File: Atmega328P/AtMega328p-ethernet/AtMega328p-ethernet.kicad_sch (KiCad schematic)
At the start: 14 parts, among them SW1 SW_Push, U1 ATmega328P-A, Y1 Crystal

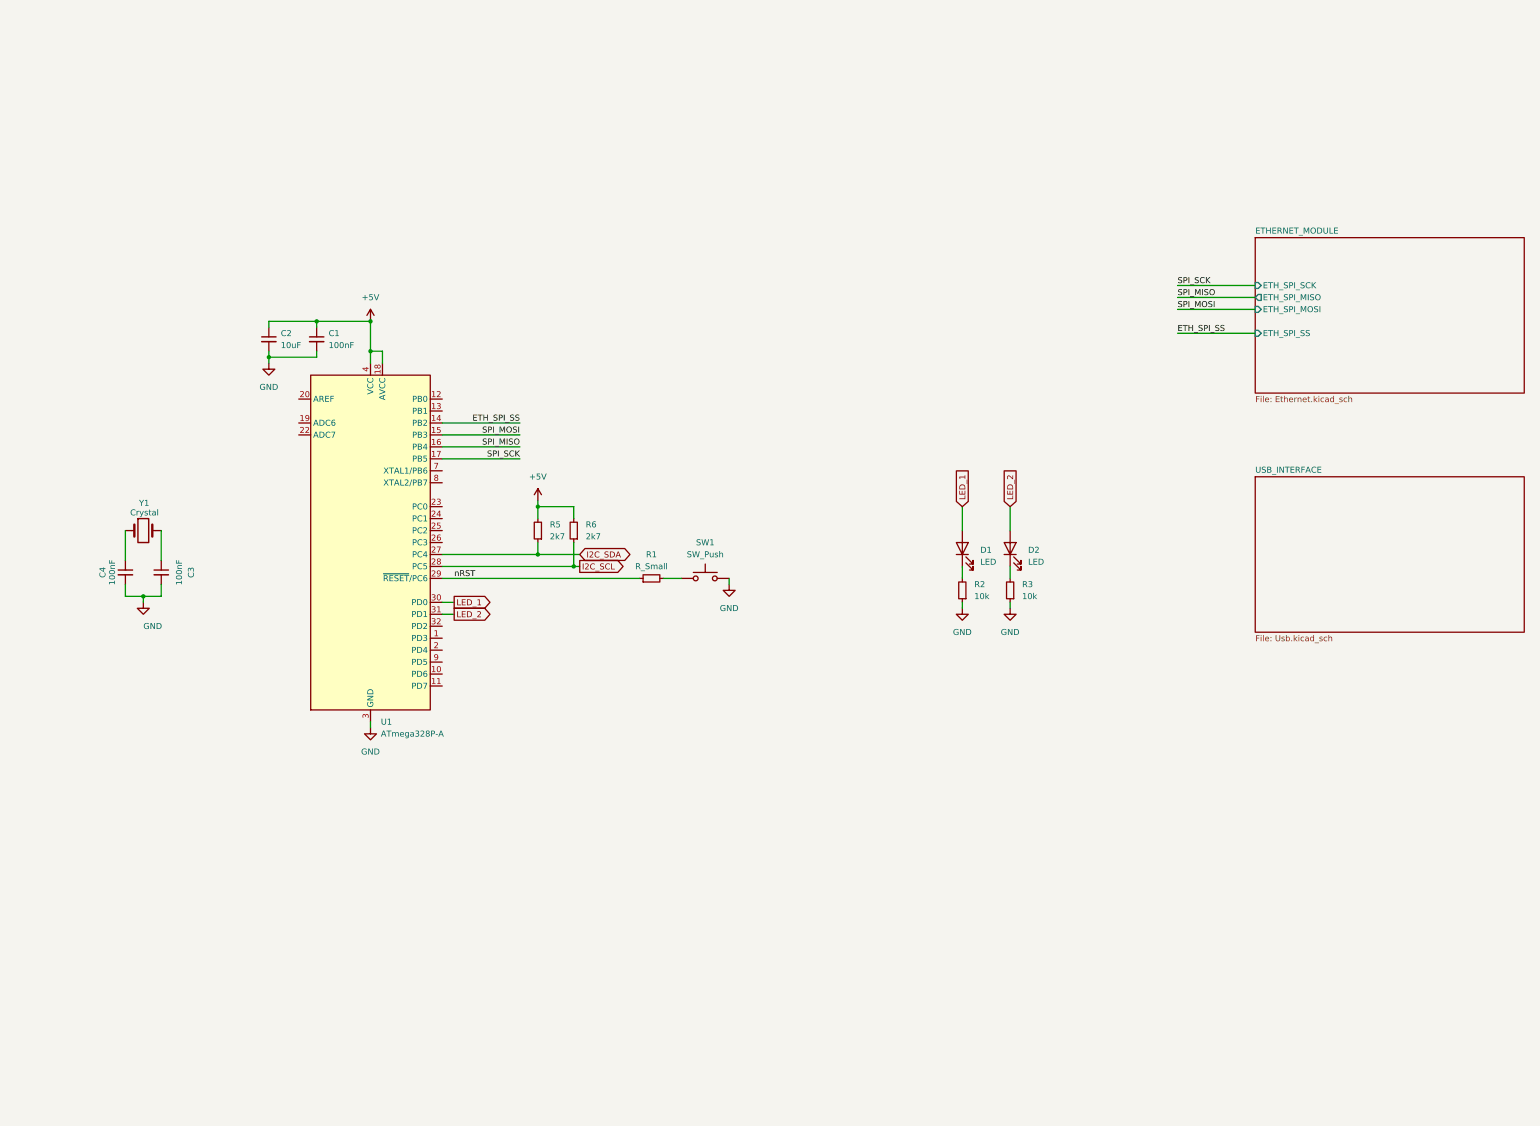
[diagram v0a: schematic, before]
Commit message: Most main components layed out
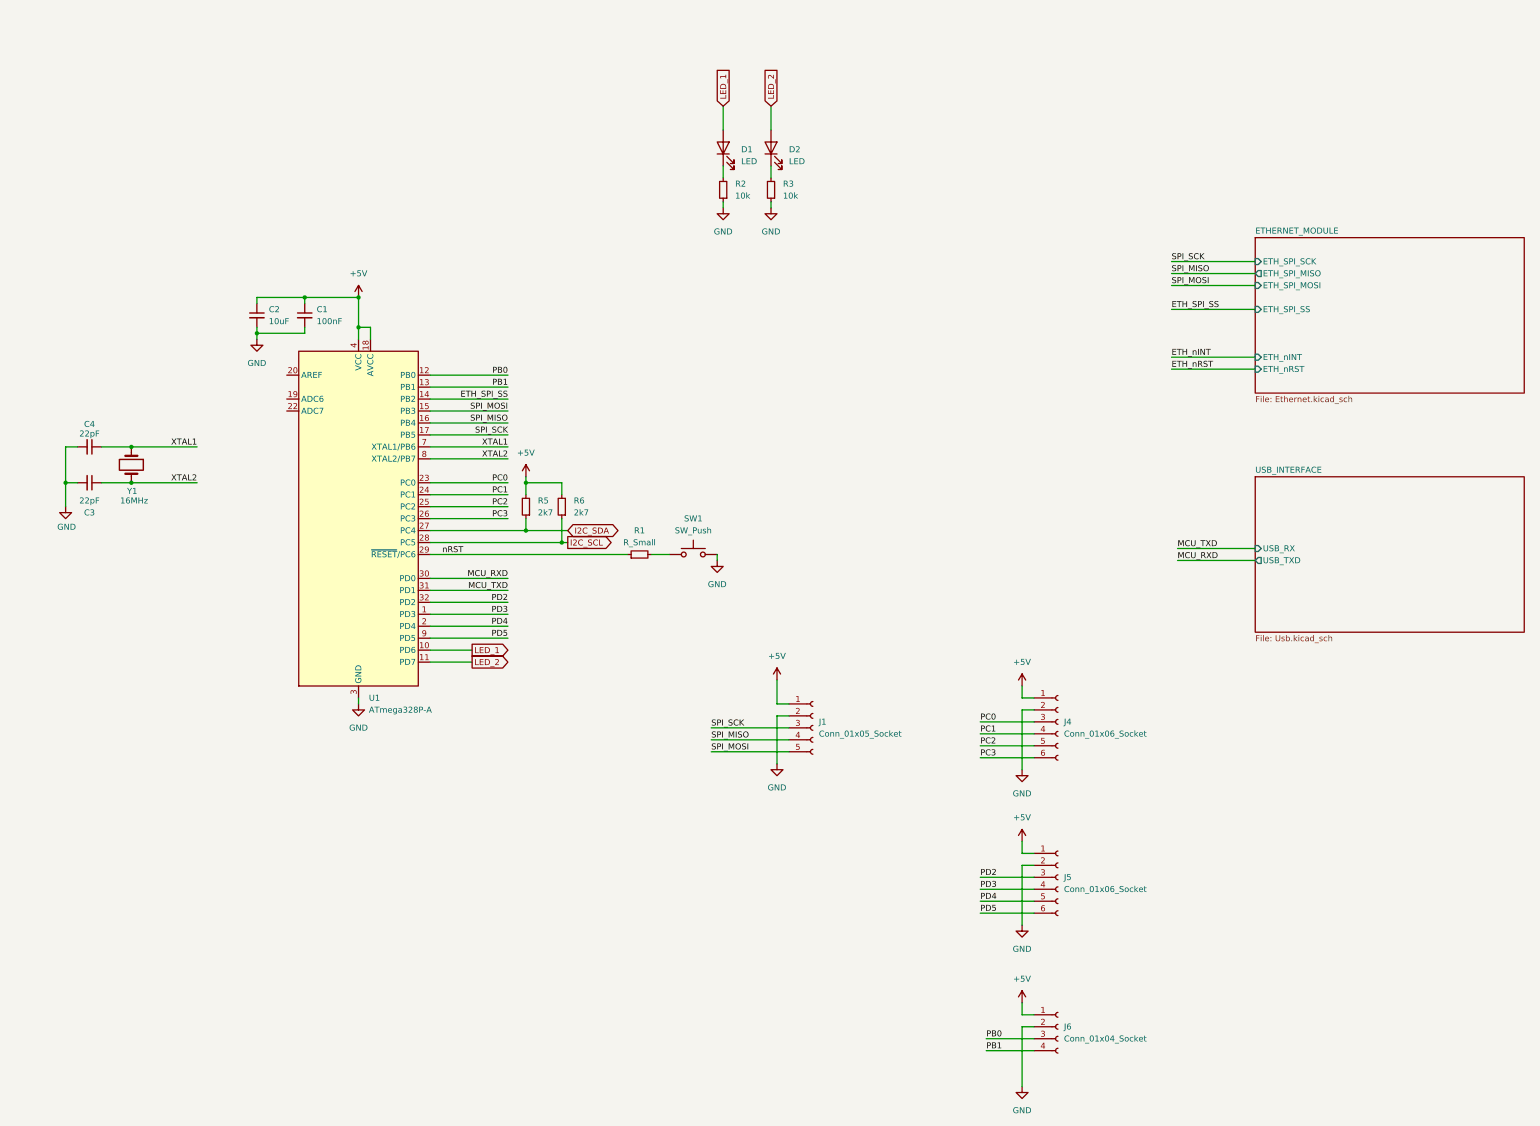
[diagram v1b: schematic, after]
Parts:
- added J1: Conn_01x05_Socket, symbol Connector:Conn_01x05_Socket
- added J4, J5: Conn_01x06_Socket, symbol Connector:Conn_01x06_Socket
- added J6: Conn_01x04_Socket, symbol Connector:Conn_01x04_Socket
- C3, C4: value 100nF -> 22pF
- Y1: value Crystal -> 16MHz
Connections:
- net +5V: now also J1.1 (Pin_1), J4.1 (Pin_1), J5.1 (Pin_1), J6.1 (Pin_1)
- net GND: now also J1.2 (Pin_2), J4.2 (Pin_2), J5.2 (Pin_2), J6.2 (Pin_2)
- net LED_1: now also U1.10 (PD6); no longer U1.30 (PD0)
- net LED_2: now also U1.11 (PD7); no longer U1.31 (PD1)
- net SPI_MISO: now also J1.4 (Pin_4)
- net SPI_MOSI: now also J1.5 (Pin_5)
- net SPI_SCK: now also J1.3 (Pin_3)
- net XTAL1: now reaches C4.1, Y1.1
- net XTAL1: now also U1.7 (XTAL1/PB6)
- net PD3: now reaches U1.1 (PD3)
- net PD3: now also J5.4 (Pin_4)
- net PB0: now reaches U1.12 (PB0)
- net PB0: now also J6.3 (Pin_3)
- net PB1: now reaches U1.13 (PB1)
- net PB1: now also J6.4 (Pin_4)
- net PD4: now reaches U1.2 (PD4)
- net PD4: now also J5.5 (Pin_5)
- net PC0: now reaches U1.23 (PC0)
- net PC0: now also J4.3 (Pin_3)
- net PC1: now reaches U1.24 (PC1)
- net PC1: now also J4.4 (Pin_4)
- net PC2: now reaches U1.25 (PC2)
- net PC2: now also J4.5 (Pin_5)
- net PC3: now reaches U1.26 (PC3)
- net PC3: now also J4.6 (Pin_6)
- net PD2: now reaches U1.32 (PD2)
- net PD2: now also J5.3 (Pin_3)
- net XTAL2: now reaches U1.8 (XTAL2/PB7)
- net XTAL2: now also C3.1, Y1.2
- net PD5: now reaches U1.9 (PD5)
- net PD5: now also J5.6 (Pin_6)
- new net MCU_RXD: U1.30 (PD0)
- new net MCU_TXD: U1.31 (PD1)
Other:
- sheet ETHERNET_MODULE ports: added ETH_nINT, ETH_nRST; removed none
- sheet USB_INTERFACE ports: added USB_RX, USB_TXD; removed none
- moved on the sheet: C1, C2, C3, C4, D1, D2, R1, R2, R3, R5, R6, SW1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

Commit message: Schematic draft complete
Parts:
- removed J6: Conn_01x04_Socket, symbol Connector:Conn_01x04_Socket
- added J6: Conn_01x06_Socket, Connector_PinHeader_1.27mm:PinHeader_1x06_P1.27mm_Vertical, symbol Connector:Conn_01x06_Socket
- added J7: Conn_01x04_Socket, Connector_PinHeader_1.27mm:PinHeader_1x04_P1.27mm_Vertical, symbol Connector:Conn_01x04_Socket
- added J8: Conn_02x03_Counter_Clockwise, Connector_PinHeader_1.27mm:PinHeader_2x03_P1.27mm_Vertical, symbol Connector_Generic:Conn_02x03_Counter_Clockwise
- C1, C3, C4: footprint (none) -> Capacitor_SMD:C_0603_1608Metric
- C2: footprint (none) -> Capacitor_SMD:CP_Elec_4x3
- D1, D2: footprint (none) -> LED_SMD:LED_0603_1608Metric
- J1: footprint (none) -> Connector_PinHeader_1.27mm:PinHeader_1x05_P1.27mm_Vertical
- J4, J5: footprint (none) -> Connector_PinHeader_1.27mm:PinHeader_1x06_P1.27mm_Vertical
- R1, R2, R3, R5, R6: footprint (none) -> Resistor_SMD:R_0603_1608Metric
- SW1: footprint (none) -> Button_Switch_SMD:SW_Push_1P1T_NO_CK_KMR2
- Y1: footprint (none) -> Crystal:Crystal_SMD_2012-2Pin_2.0x1.2mm
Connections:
- net +5V: now also J6.1 (Pin_1), J7.1 (Pin_1), J8.6 (Pin_6)
- net GND: now also J6.2 (Pin_2), J7.2 (Pin_2), J8.4 (Pin_4)
- net MCU_RXD: now also J7.3 (Pin_3)
- net MCU_TXD: now also J7.4 (Pin_4)
- net PB0: now also J6.3 (Pin_3)
- net PB1: now also J6.4 (Pin_4)
- net SPI_MISO: now also J8.1 (Pin_1)
- net SPI_MOSI: now also J8.5 (Pin_5)
- net SPI_SCK: now also J8.2 (Pin_2)
- net nRST: now also J8.3 (Pin_3)
- net LED_1 renamed PD6/LED1
- net PD6/LED1: now also J6.5 (Pin_5)
- net LED_2 renamed PD7/LED2
- net PD7/LED2: now also J6.6 (Pin_6)
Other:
- added sheet POWER SUPPLIES (Power.kicad_sch)
- company: (none) -> HUNTER INC.
- title: (none) -> MAIN SHEET
- moved on the sheet: C1, C2, C3, C4, D1, D2, R1, R2, R3, R5, R6, SW1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

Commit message: PCB Layout done initial
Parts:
- removed J7: Conn_01x04_Socket, Connector_PinHeader_1.27mm:PinHeader_1x04_P1.27mm_Vertical, symbol Connector:Conn_01x04_Socket
- added J7: Conn_01x06_Socket, Connector_PinHeader_2.54mm:PinHeader_1x06_P2.54mm_Vertical, symbol Connector:Conn_01x06_Socket
- J1: footprint Connector_PinHeader_1.27mm:PinHeader_1x05_P1.27mm_Vertical -> Connector_PinHeader_2.54mm:PinHeader_1x05_P2.54mm_Vertical
- J4, J5, J6: footprint Connector_PinHeader_1.27mm:PinHeader_1x06_P1.27mm_Vertical -> Connector_PinHeader_2.54mm:PinHeader_1x06_P2.54mm_Vertical
- J8: footprint Connector_PinHeader_1.27mm:PinHeader_2x03_P1.27mm_Vertical -> Connector_PinHeader_2.54mm:PinHeader_2x03_P2.54mm_Vertical
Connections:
- net +5V: now also J7.1 (Pin_1)
- net GND: now also J7.2 (Pin_2)
- net I2C_SCL: now also J7.6 (Pin_6)
- net I2C_SDA: now also J7.5 (Pin_5)
- net MCU_RXD: now also J7.3 (Pin_3)
- net MCU_TXD: now also J7.4 (Pin_4)
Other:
- moved on the sheet: J1

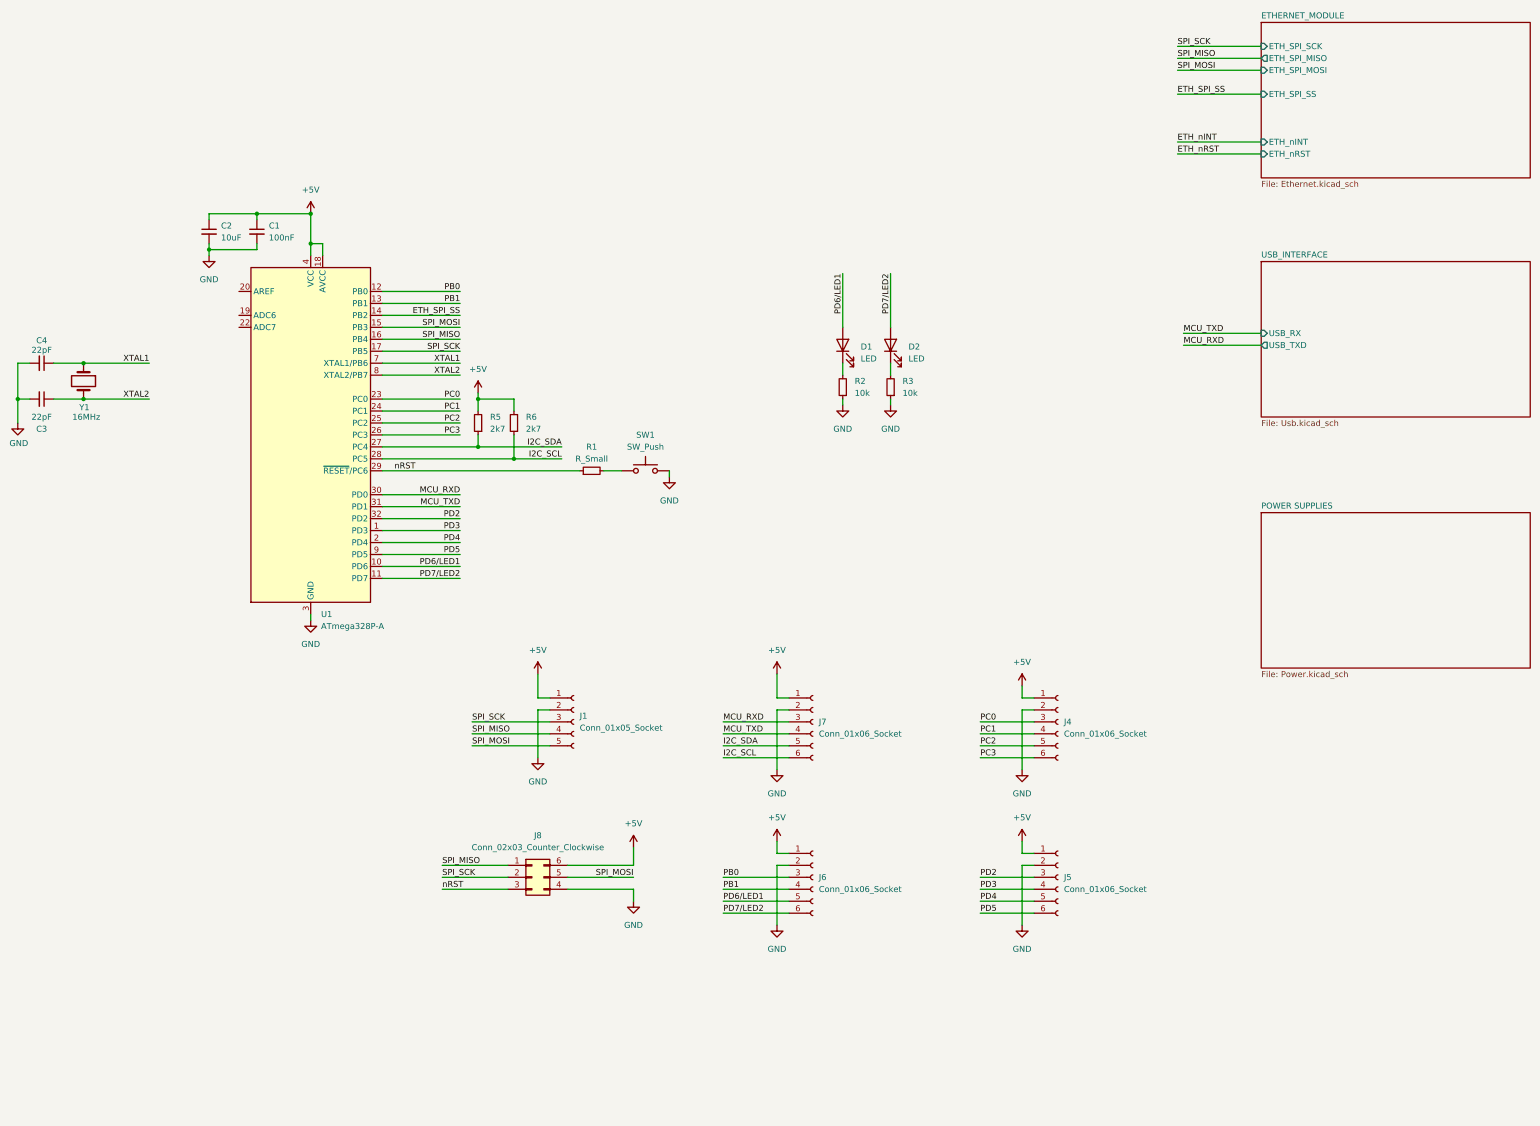
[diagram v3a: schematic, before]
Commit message: Added dif pair and finished USB schematic
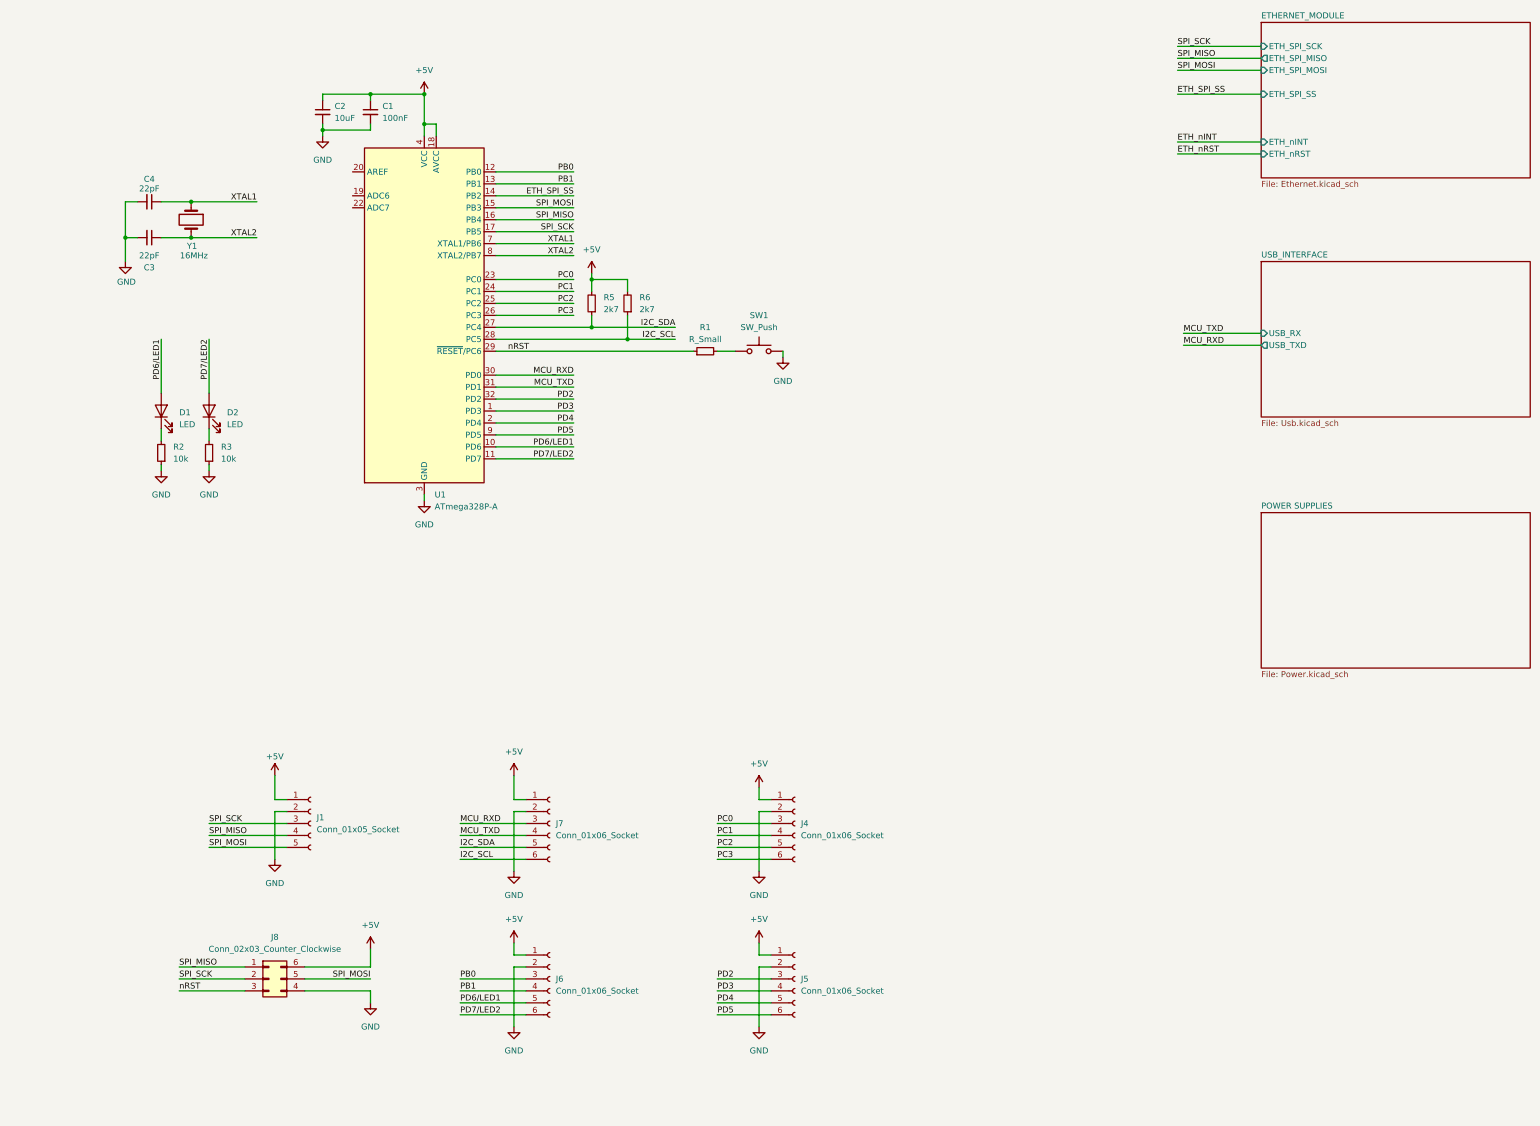
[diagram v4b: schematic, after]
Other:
- moved on the sheet: C1, C2, C3, C4, D1, D2, J1, J4, J5, J6, J7, J8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
